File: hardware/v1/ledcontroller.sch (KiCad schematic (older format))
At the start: 4 parts, among them U1 MAX7221

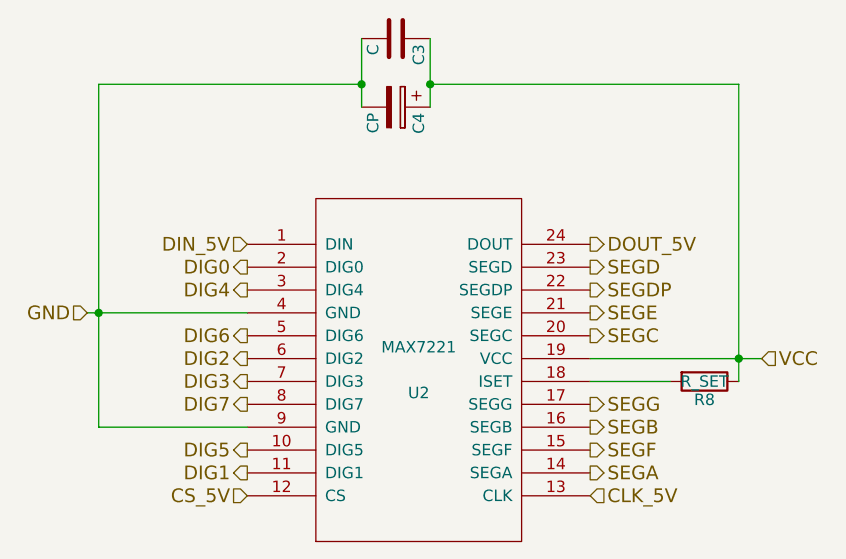
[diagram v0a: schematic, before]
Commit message: Add keys-8 schematic and initial pcb layout file.
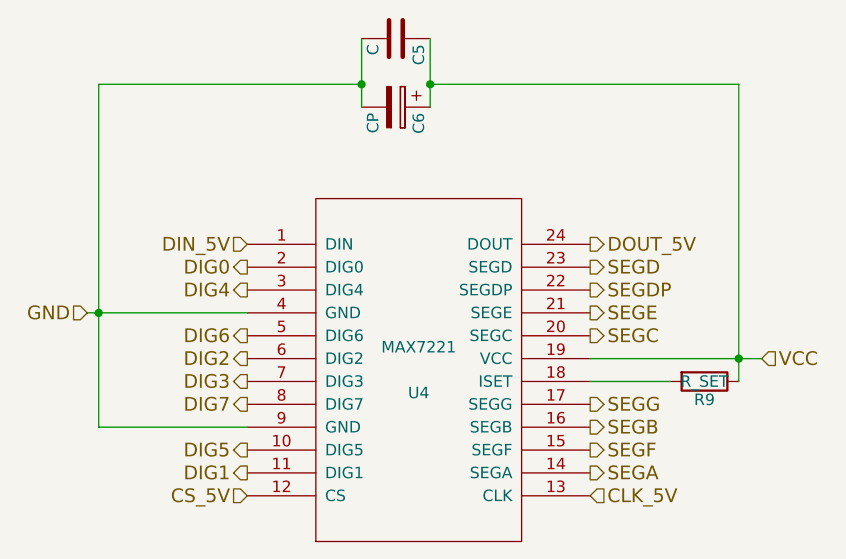
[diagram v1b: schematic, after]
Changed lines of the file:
@@
 $Descr A4 11693 8268
 encoding utf-8
-Sheet 6 25
+Sheet 6 26
 Title ""
 Date ""
@@
 AR Path="/57A2FF40/57A5D8B0/57A34228" Ref="U2"  Part="1"
 AR Path="/57A30207/57A34228" Ref="U4"  Part="1"
-F 0 "U2" H 5750 3500 50  0000 C CNN
+F 0 "U4" H 5750 3500 50  0000 C CNN
 F 1 "MAX7221" H 5750 3700 50  0000 C CNN
 F 2 "DIL24:DIL24" H 5750 3600 50  0001 C CNN
@@
 AR Path="/57A2FF40/57A5D8B0/57A343D9" Ref="R8"  Part="1"
 AR Path="/57A30207/57A343D9" Ref="R9"  Part="1"
-F 0 "R8" V 7080 3650 50  0000 C CNN
+F 0 "R9" V 7080 3650 50  0000 C CNN
 F 1 "R_SET" V 7000 3650 50  0000 C CNN
 F 2 "Resistors_ThroughHole:Resistor_Horizontal_RM10mm" V 6930 3650 50  0001 C CNN
@@
 AR Path="/57A2FF40/57A5D8B0/57A3585E" Ref="C3"  Part="1"
 AR Path="/57A30207/57A3585E" Ref="C5"  Part="1"
-F 0 "C3" H 5675 2250 50  0000 L CNN
+F 0 "C5" H 5675 2250 50  0000 L CNN
 F 1 "C" H 5675 2050 50  0000 L CNN
 F 2 "Capacitors_ThroughHole:C_Disc_D6_P5" H 5688 2000 50  0001 C CNN
@@
 AR Path="/57A2FF40/57A5D8B0/57A358C3" Ref="C4"  Part="1"
 AR Path="/57A30207/57A358C3" Ref="C6"  Part="1"
-F 0 "C4" H 5675 2550 50  0000 L CNN
+F 0 "C6" H 5675 2550 50  0000 L CNN
 F 1 "CP" H 5675 2350 50  0000 L CNN
 F 2 "Discret:CP36V" H 5688 2300 50  0001 C CNN

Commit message: Assign DP pin to led0 connection to match 8-bit values in MAX7221 register.
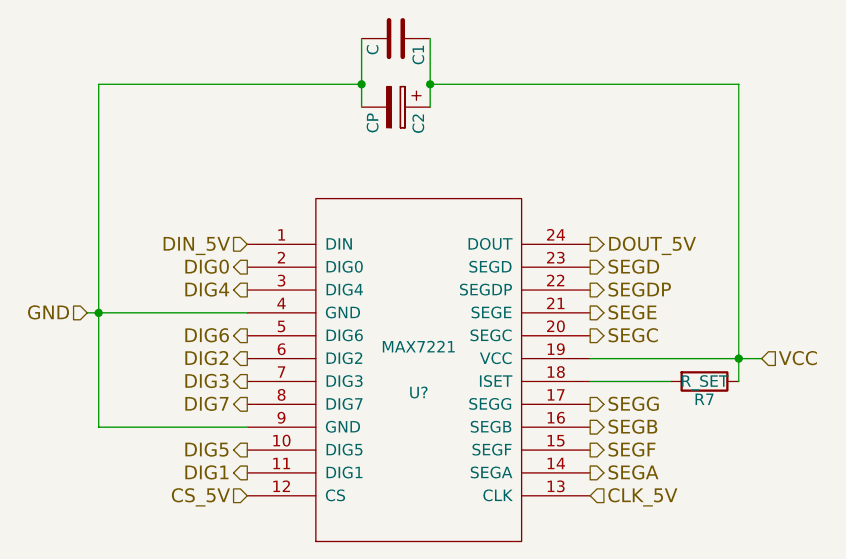
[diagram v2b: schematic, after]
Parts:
- renumbered U1 to U?
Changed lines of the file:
@@
 LIBS:contrib
 LIBS:valves
+LIBS:Pi2_Connector
 LIBS:MAX7221
 LIBS:MCP23S17
 LIBS:MCP23017
-LIBS:Pi2_Connector
-LIBS:v1-cache
+LIBS:piconnect-cache
 EELAYER 25 0
 EELAYER END
 $Descr A4 11693 8268
 encoding utf-8
-Sheet 6 26
+Sheet 6 6
 Title ""
 Date ""
@@
 $EndDescr
 $Comp
-L MAX7221 U1
+L MAX7221 U?
 U 1 1 57A34228
 P 5750 3600
-AR Path="/57A2FF40/57A5CF2B/57A34228" Ref="U1"  Part="1"
-AR Path="/57A2FF40/57A5D8B0/57A34228" Ref="U2"  Part="1"
-AR Path="/57A30207/57A34228" Ref="U4"  Part="1"
-F 0 "U4" H 5750 3500 50  0000 C CNN
+AR Path="/57A5CF2B/57A34228" Ref="U?"  Part="1"
+AR Path="/57A5D8B0/57A34228" Ref="U?"  Part="1"
+F 0 "U?" H 5750 3500 50  0000 C CNN
 F 1 "MAX7221" H 5750 3700 50  0000 C CNN
 F 2 "DIL24:DIL24" H 5750 3600 50  0001 C CNN
@@
 U 1 1 57A343D9
 P 7000 3650
-AR Path="/57A2FF40/57A5CF2B/57A343D9" Ref="R7"  Part="1"
-AR Path="/57A2FF40/57A5D8B0/57A343D9" Ref="R8"  Part="1"
-AR Path="/57A30207/57A343D9" Ref="R9"  Part="1"
-F 0 "R9" V 7080 3650 50  0000 C CNN
+AR Path="/57A5CF2B/57A343D9" Ref="R7"  Part="1"
+AR Path="/57A5D8B0/57A343D9" Ref="R8"  Part="1"
+F 0 "R7" V 7080 3650 50  0000 C CNN
 F 1 "R_SET" V 7000 3650 50  0000 C CNN
 F 2 "Resistors_ThroughHole:Resistor_Horizontal_RM10mm" V 6930 3650 50  0001 C CNN
@@
 U 1 1 57A3585E
 P 5650 2150
-AR Path="/57A2FF40/57A5CF2B/57A3585E" Ref="C1"  Part="1"
-AR Path="/57A2FF40/57A5D8B0/57A3585E" Ref="C3"  Part="1"
-AR Path="/57A30207/57A3585E" Ref="C5"  Part="1"
-F 0 "C5" H 5675 2250 50  0000 L CNN
+AR Path="/57A5CF2B/57A3585E" Ref="C1"  Part="1"
+AR Path="/57A5D8B0/57A3585E" Ref="C3"  Part="1"
+F 0 "C1" H 5675 2250 50  0000 L CNN
 F 1 "C" H 5675 2050 50  0000 L CNN
 F 2 "Capacitors_ThroughHole:C_Disc_D6_P5" H 5688 2000 50  0001 C CNN
@@
 U 1 1 57A358C3
 P 5650 2450
-AR Path="/57A2FF40/57A5CF2B/57A358C3" Ref="C2"  Part="1"
-AR Path="/57A2FF40/57A5D8B0/57A358C3" Ref="C4"  Part="1"
-AR Path="/57A30207/57A358C3" Ref="C6"  Part="1"
-F 0 "C6" H 5675 2550 50  0000 L CNN
+AR Path="/57A5CF2B/57A358C3" Ref="C2"  Part="1"
+AR Path="/57A5D8B0/57A358C3" Ref="C4"  Part="1"
+F 0 "C2" H 5675 2550 50  0000 L CNN
 F 1 "CP" H 5675 2350 50  0000 L CNN
 F 2 "Discret:CP36V" H 5688 2300 50  0001 C CNN

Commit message: Add new schematics for additional switch boards
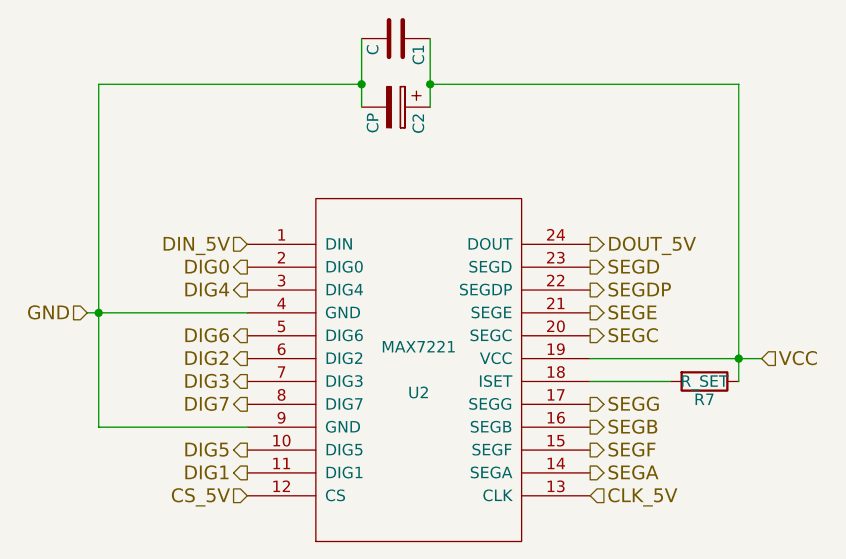
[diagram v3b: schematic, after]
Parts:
- gave numbers to parts that had none: 1
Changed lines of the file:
@@
 LIBS:contrib
 LIBS:valves
-LIBS:Pi2_Connector
 LIBS:MAX7221
 LIBS:MCP23S17
 LIBS:MCP23017
-LIBS:piconnect-cache
+LIBS:Pi2_Connector
+LIBS:v1-cache
 EELAYER 25 0
 EELAYER END
 $Descr A4 11693 8268
 encoding utf-8
-Sheet 6 6
+Sheet 6 30
 Title ""
 Date ""
@@
 $EndDescr
 $Comp
-L MAX7221 U?
+L MAX7221 U2
 U 1 1 57A34228
 P 5750 3600
-AR Path="/57A5CF2B/57A34228" Ref="U?"  Part="1"
-AR Path="/57A5D8B0/57A34228" Ref="U?"  Part="1"
-F 0 "U?" H 5750 3500 50  0000 C CNN
+AR Path="/57A2FF40/57A5CF2B/57A34228" Ref="U2"  Part="1"
+AR Path="/57A2FF40/57A5D8B0/57A34228" Ref="U3"  Part="1"
+AR Path="/57A30207/57A34228" Ref="U5"  Part="1"
+F 0 "U2" H 5750 3500 50  0000 C CNN
 F 1 "MAX7221" H 5750 3700 50  0000 C CNN
 F 2 "DIL24:DIL24" H 5750 3600 50  0001 C CNN
@@
 U 1 1 57A343D9
 P 7000 3650
-AR Path="/57A5CF2B/57A343D9" Ref="R7"  Part="1"
-AR Path="/57A5D8B0/57A343D9" Ref="R8"  Part="1"
+AR Path="/57A2FF40/57A5CF2B/57A343D9" Ref="R7"  Part="1"
+AR Path="/57A2FF40/57A5D8B0/57A343D9" Ref="R8"  Part="1"
+AR Path="/57A30207/57A343D9" Ref="R9"  Part="1"
 F 0 "R7" V 7080 3650 50  0000 C CNN
 F 1 "R_SET" V 7000 3650 50  0000 C CNN
@@
 U 1 1 57A3585E
 P 5650 2150
-AR Path="/57A5CF2B/57A3585E" Ref="C1"  Part="1"
-AR Path="/57A5D8B0/57A3585E" Ref="C3"  Part="1"
+AR Path="/57A2FF40/57A5CF2B/57A3585E" Ref="C1"  Part="1"
+AR Path="/57A2FF40/57A5D8B0/57A3585E" Ref="C3"  Part="1"
+AR Path="/57A30207/57A3585E" Ref="C5"  Part="1"
 F 0 "C1" H 5675 2250 50  0000 L CNN
 F 1 "C" H 5675 2050 50  0000 L CNN
@@
 U 1 1 57A358C3
 P 5650 2450
-AR Path="/57A5CF2B/57A358C3" Ref="C2"  Part="1"
-AR Path="/57A5D8B0/57A358C3" Ref="C4"  Part="1"
+AR Path="/57A2FF40/57A5CF2B/57A358C3" Ref="C2"  Part="1"
+AR Path="/57A2FF40/57A5D8B0/57A358C3" Ref="C4"  Part="1"
+AR Path="/57A30207/57A358C3" Ref="C6"  Part="1"
 F 0 "C2" H 5675 2550 50  0000 L CNN
 F 1 "CP" H 5675 2350 50  0000 L CNN
